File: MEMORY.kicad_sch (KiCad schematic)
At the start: 6 parts, among them IC1 ECP5-BGA256, U6 S27KL0641, U7 SI5351A-B-GTR, Y1 Crystal_GND24

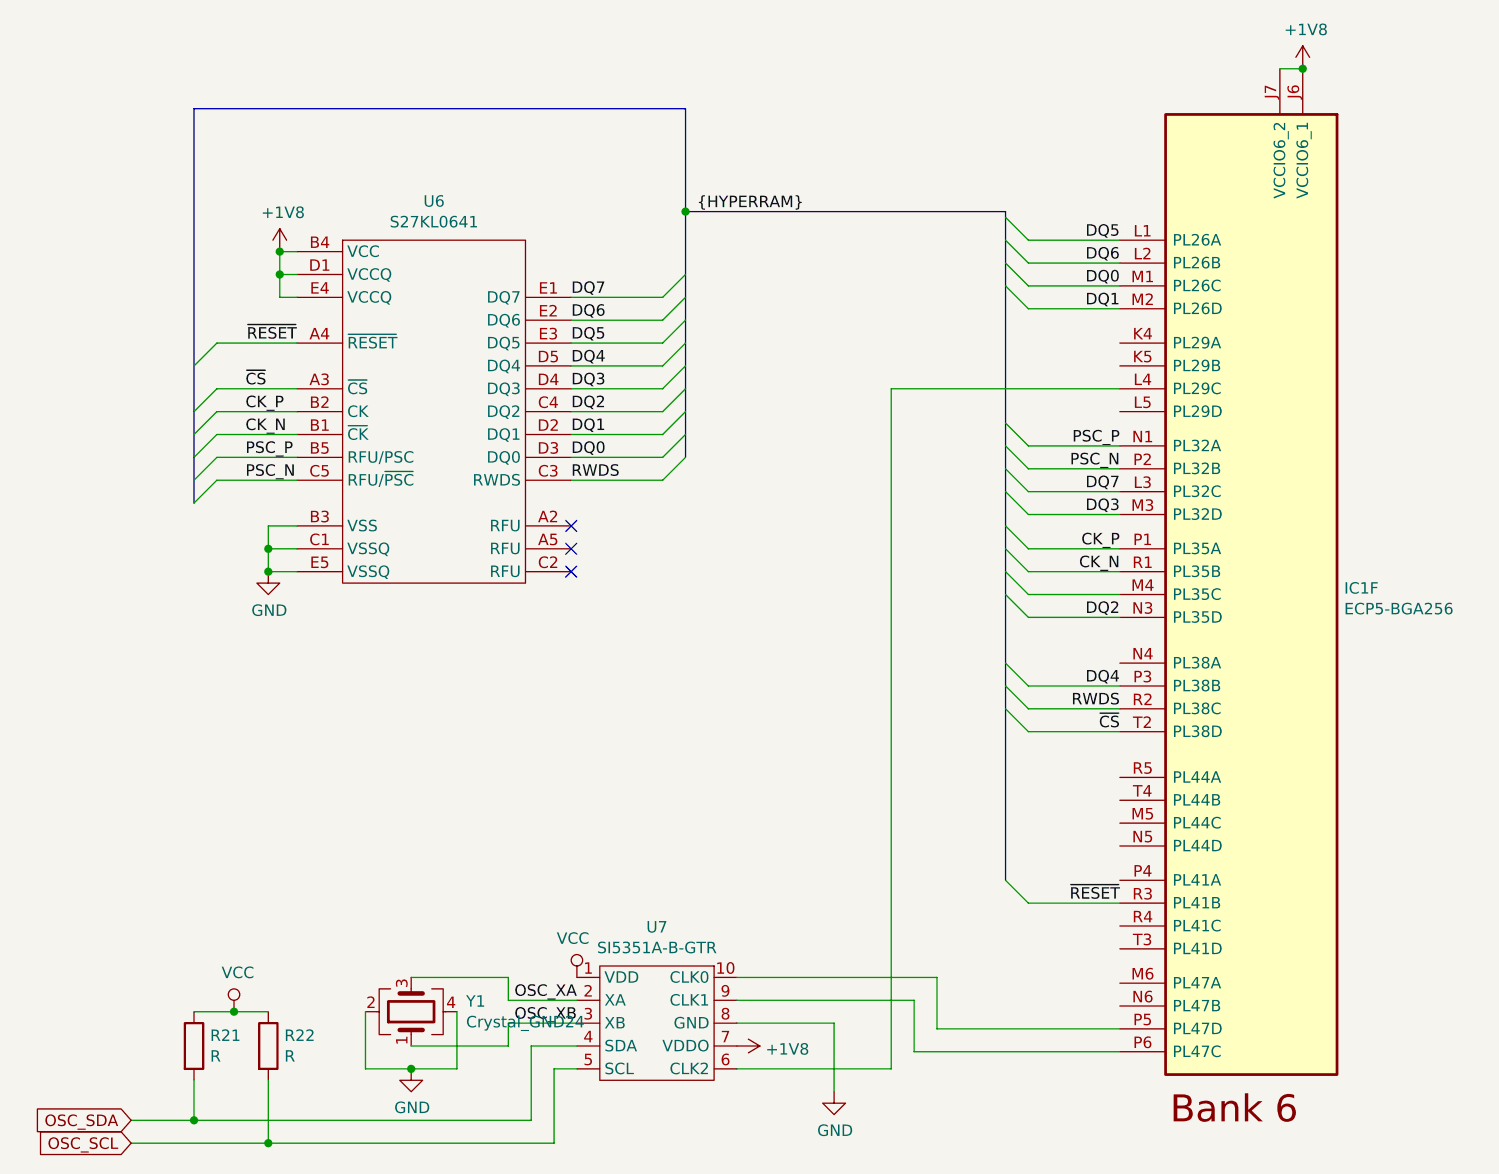
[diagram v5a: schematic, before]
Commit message: Remove SD card, relocate regulators
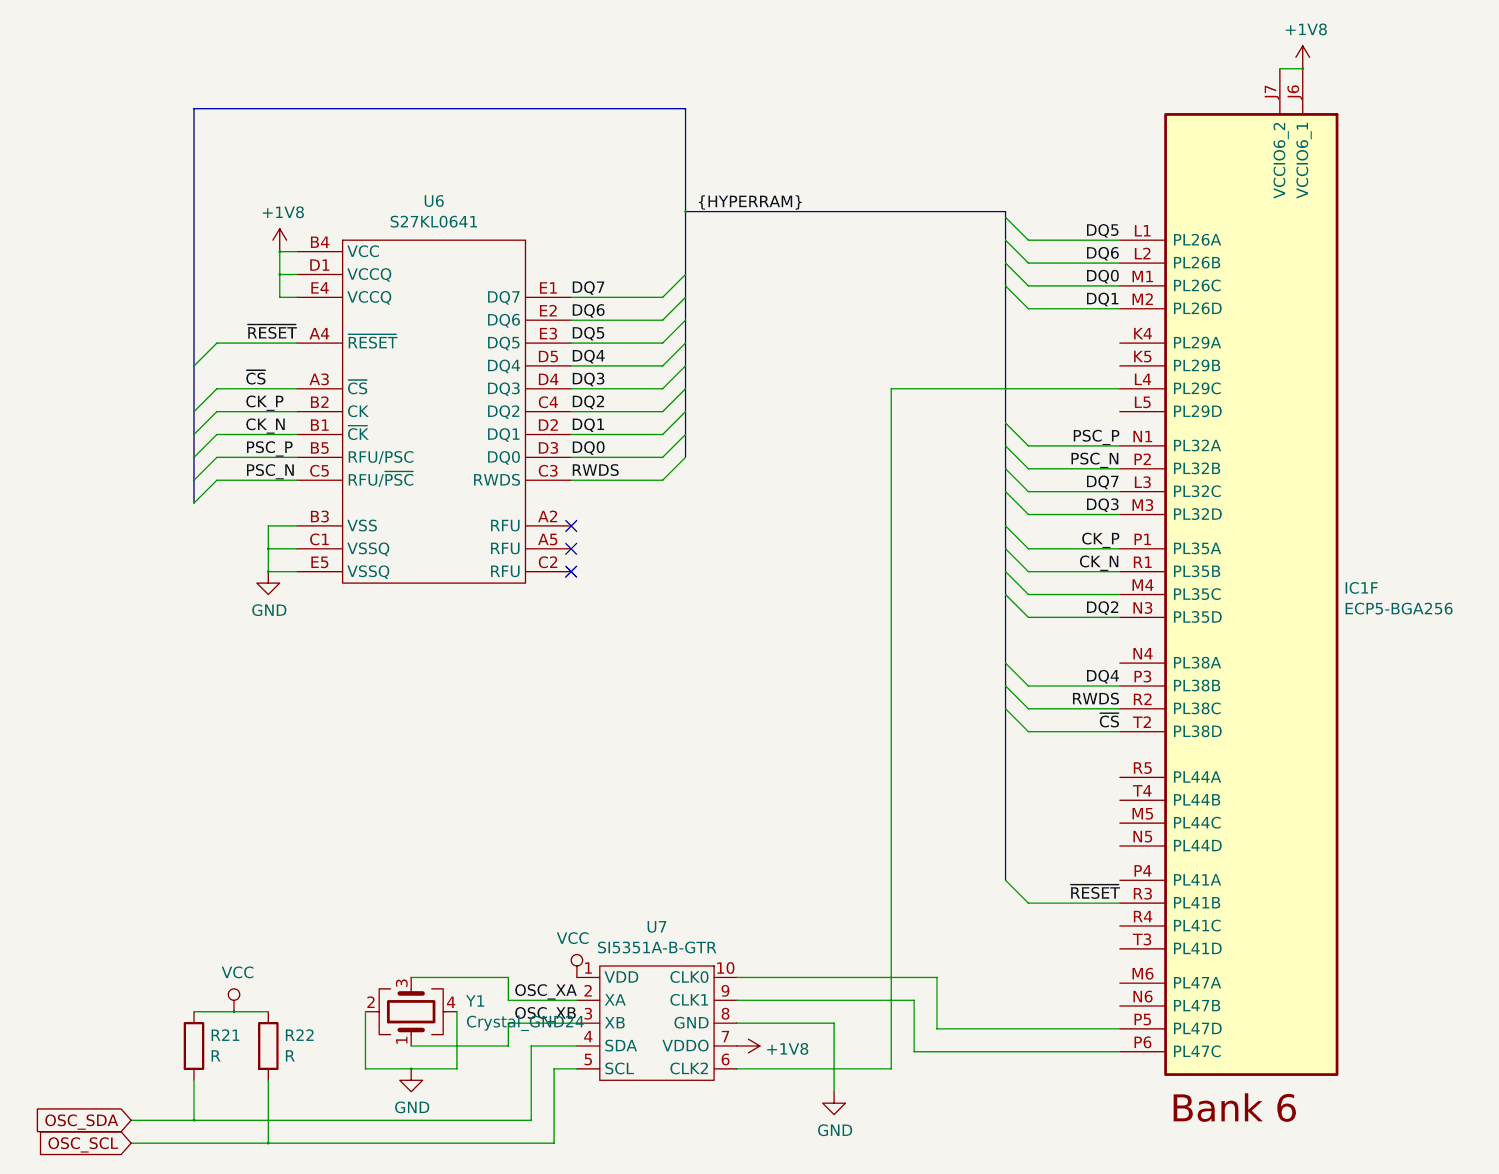
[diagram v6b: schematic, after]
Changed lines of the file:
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@@
-(kicad_sch (version 20200714) (host eeschema "5.99.0-unknown-8324cb3~102~ubuntu20.04.1")
-  (page 1 6)
+(kicad_sch (version 20200714) (host eeschema "5.99.0-unknown-027b6c8cf~102~ubuntu20.04.1")
+  (page 3 6)
   (paper "A4")
   (bus_alias "HYPERRAM" (members "DQ[0..7]" "RWDS" "~CS" "CK_N" "CK_P" "PSC_N" "PSC_P" "~RESET"))
-  (junction (at 97.155 153.67) (diameter 0) (color 0 0 0 0))
-  (junction (at 101.6 141.605) (diameter 0) (color 0 0 0 0))
-  (junction (at 105.41 90.17) (diameter 0) (color 0 0 0 0))
-  (junction (at 105.41 92.71) (diameter 0) (color 0 0 0 0))
-  (junction (at 105.41 156.21) (diameter 0) (color 0 0 0 0))
-  (junction (at 106.68 57.15) (diameter 0) (color 0 0 0 0))
-  (junction (at 106.68 59.69) (diameter 0) (color 0 0 0 0))
-  (junction (at 121.285 147.955) (diameter 0) (color 0 0 0 0))
-  (junction (at 220.345 36.83) (diameter 0) (color 0 0 0 0))
-  (junction (at 151.765 52.705) (diameter 0) (color 0 0 0 0))
+  (junction (at 97.155 153.67) (diameter 0.3048) (color 0 0 0 0))
+  (junction (at 101.6 141.605) (diameter 0.3048) (color 0 0 0 0))
+  (junction (at 105.41 90.17) (diameter 0.3048) (color 0 0 0 0))
+  (junction (at 105.41 92.71) (diameter 0.3048) (color 0 0 0 0))
+  (junction (at 105.41 156.21) (diameter 0.3048) (color 0 0 0 0))
+  (junction (at 106.68 57.15) (diameter 0.3048) (color 0 0 0 0))
+  (junction (at 106.68 59.69) (diameter 0.3048) (color 0 0 0 0))
+  (junction (at 121.285 147.955) (diameter 0.3048) (color 0 0 0 0))
+  (junction (at 220.345 36.83) (diameter 0.3048) (color 0 0 0 0))
+  (junction (at 151.765 52.705) (diameter 0.3048) (color 0 0 0 0))
   (no_connect (at 139.065 87.63))
   (no_connect (at 139.065 92.71))
@@
     (stroke (width 0) (type solid) (color 0 0 0 0))
   )
-  (bus (pts (xy 97.155 41.275) (xy 97.155 74.93))
-    (stroke (width 0) (type solid) (color 0 0 0 0))
-  )
-  (bus (pts (xy 97.155 74.93) (xy 97.155 80.01))
-    (stroke (width 0) (type solid) (color 0 0 0 0))
-  )
-  (bus (pts (xy 97.155 80.01) (xy 97.155 85.09))
+  (bus (pts (xy 97.155 41.275) (xy 97.155 69.85))
+    (stroke (width 0) (type solid) (color 0 0 0 0))
+  )
+  (bus (pts (xy 97.155 69.85) (xy 97.155 74.93))
+    (stroke (width 0) (type solid) (color 0 0 0 0))
+  )
+  (bus (pts (xy 97.155 74.93) (xy 97.155 77.47))
+    (stroke (width 0) (type solid) (color 0 0 0 0))
+  )
+  (bus (pts (xy 97.155 77.47) (xy 97.155 80.01))
+    (stroke (width 0) (type solid) (color 0 0 0 0))
+  )
+  (bus (pts (xy 97.155 80.01) (xy 97.155 82.55))
+    (stroke (width 0) (type solid) (color 0 0 0 0))
+  )
+  (bus (pts (xy 97.155 82.55) (xy 97.155 85.09))
     (stroke (width 0) (type solid) (color 0 0 0 0))
   )
@@
     (stroke (width 0) (type solid) (color 0 0 0 0))
   )
-  (bus (pts (xy 151.765 52.705) (xy 151.765 62.23))
+  (bus (pts (xy 151.765 52.705) (xy 151.765 59.69))
     (stroke (width 0) (type solid) (color 0 0 0 0))
   )
@@
     (stroke (width 0) (type solid) (color 0 0 0 0))
   )
-  (bus (pts (xy 151.765 62.23) (xy 151.765 67.31))
-    (stroke (width 0) (type solid) (color 0 0 0 0))
-  )
-  (bus (pts (xy 151.765 67.31) (xy 151.765 72.39))
-    (stroke (width 0) (type solid) (color 0 0 0 0))
-  )
-  (bus (pts (xy 151.765 72.39) (xy 151.765 77.47))
+  (bus (pts (xy 151.765 59.69) (xy 151.765 62.23))
+    (stroke (width 0) (type solid) (color 0 0 0 0))
+  )
+  (bus (pts (xy 151.765 62.23) (xy 151.765 64.77))
+    (stroke (width 0) (type solid) (color 0 0 0 0))
+  )
+  (bus (pts (xy 151.765 64.77) (xy 151.765 67.31))
+    (stroke (width 0) (type solid) (color 0 0 0 0))
+  )
+  (bus (pts (xy 151.765 67.31) (xy 151.765 69.85))
+    (stroke (width 0) (type solid) (color 0 0 0 0))
+  )
+  (bus (pts (xy 151.765 69.85) (xy 151.765 72.39))
+    (stroke (width 0) (type solid) (color 0 0 0 0))
+  )
+  (bus (pts (xy 151.765 72.39) (xy 151.765 74.93))
+    (stroke (width 0) (type solid) (color 0 0 0 0))
+  )
+  (bus (pts (xy 151.765 74.93) (xy 151.765 77.47))
     (stroke (width 0) (type solid) (color 0 0 0 0))
   )
@@
     (stroke (width 0) (type solid) (color 0 0 0 0))
   )
-  (bus (pts (xy 187.325 52.705) (xy 187.325 55.88))
-    (stroke (width 0) (type solid) (color 0 0 0 0))
-  )
-  (bus (pts (xy 187.325 55.88) (xy 187.325 60.96))
+  (bus (pts (xy 187.325 52.705) (xy 187.325 53.34))
+    (stroke (width 0) (type solid) (color 0 0 0 0))
+  )
+  (bus (pts (xy 187.325 53.34) (xy 187.325 55.88))
+    (stroke (width 0) (type solid) (color 0 0 0 0))
+  )
+  (bus (pts (xy 187.325 55.88) (xy 187.325 58.42))
+    (stroke (width 0) (type solid) (color 0 0 0 0))
+  )
+  (bus (pts (xy 187.325 58.42) (xy 187.325 60.96))
     (stroke (width 0) (type solid) (color 0 0 0 0))
   )
@@
     (stroke (width 0) (type solid) (color 0 0 0 0))
   )
-  (bus (pts (xy 187.325 76.2) (xy 187.325 81.28))
-    (stroke (width 0) (type solid) (color 0 0 0 0))
-  )
-  (bus (pts (xy 187.325 81.28) (xy 187.325 87.63))
-    (stroke (width 0) (type solid) (color 0 0 0 0))
-  )
-  (bus (pts (xy 187.325 87.63) (xy 187.325 92.71))
+  (bus (pts (xy 187.325 76.2) (xy 187.325 78.74))
+    (stroke (width 0) (type solid) (color 0 0 0 0))
+  )
+  (bus (pts (xy 187.325 78.74) (xy 187.325 81.28))
+    (stroke (width 0) (type solid) (color 0 0 0 0))
+  )
+  (bus (pts (xy 187.325 81.28) (xy 187.325 83.82))
+    (stroke (width 0) (type solid) (color 0 0 0 0))
+  )
+  (bus (pts (xy 187.325 83.82) (xy 187.325 87.63))
+    (stroke (width 0) (type solid) (color 0 0 0 0))
+  )
+  (bus (pts (xy 187.325 87.63) (xy 187.325 90.17))
+    (stroke (width 0) (type solid) (color 0 0 0 0))
+  )
+  (bus (pts (xy 187.325 90.17) (xy 187.325 92.71))
     (stroke (width 0) (type solid) (color 0 0 0 0))
   )
@@
     (stroke (width 0) (type solid) (color 0 0 0 0))
   )
-  (bus (pts (xy 187.325 95.25) (xy 187.325 105.41))
-    (stroke (width 0) (type solid) (color 0 0 0 0))
-  )
-  (bus (pts (xy 187.325 105.41) (xy 187.325 127))
-    (stroke (width 0) (type solid) (color 0 0 0 0))
-  )
+  (bus (pts (xy 187.325 95.25) (xy 187.325 102.87))
+    (stroke (width 0) (type solid) (color 0 0 0 0))
+  )
+  (bus (pts (xy 187.325 102.87) (xy 187.325 105.41))
+    (stroke (width 0) (type solid) (color 0 0 0 0))
+  )
+  (bus (pts (xy 187.325 105.41) (xy 187.325 107.95))
+    (stroke (width 0) (type solid) (color 0 0 0 0))
+  )
+  (bus (pts (xy 187.325 107.95) (xy 187.325 127))
+    (stroke (width 0) (type solid) (color 0 0 0 0))
+  )
